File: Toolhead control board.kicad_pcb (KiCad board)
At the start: 2 copper layers, 52 x 45.8 mm, 77 parts, among them J1 Conn_01x02_Pin, J12 Conn_01x04_Male, J14 Conn_01x04_Male, J2 Conn_01x02_Pin, J3 Conn_01x02_Pin, J4 Conn_01x02_Pin, J5 Conn_01x02_Pin, J6 Conn_01x02_Pin, J7 USB_C_Receptacle_USB2.0_14P, Q1 AS3400, Q2 AS3400, Q3 AS3400, SW1 SW_SPST, SW2 SW_SPST, U1 ADXL345, U2 STM32F042G6Ux, U3 TMC2209, U4 AP63205WU, U5 MCP1802x-xx02xOT, U6 LP5907-2.5, Y1 8MHz

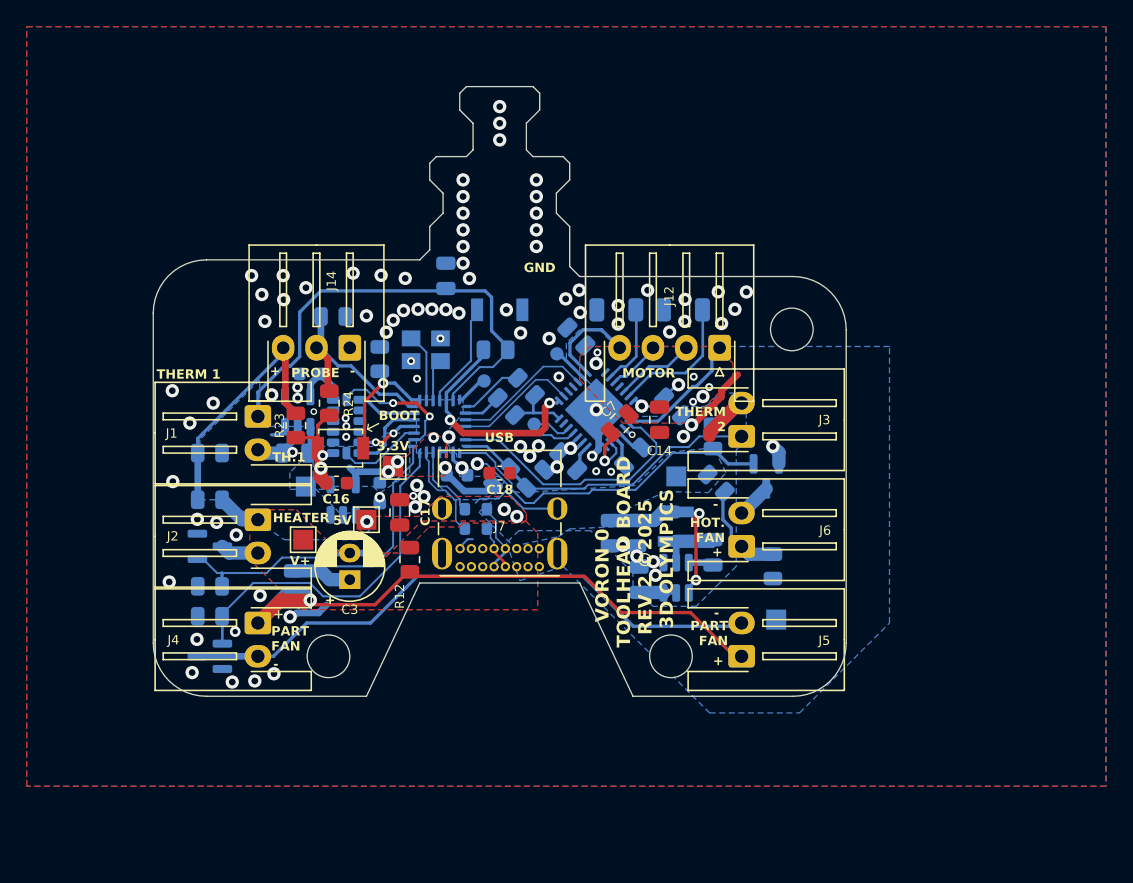
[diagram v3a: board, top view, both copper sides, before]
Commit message: Rev3 (connectors on back, and with USB daughter board) - probably done
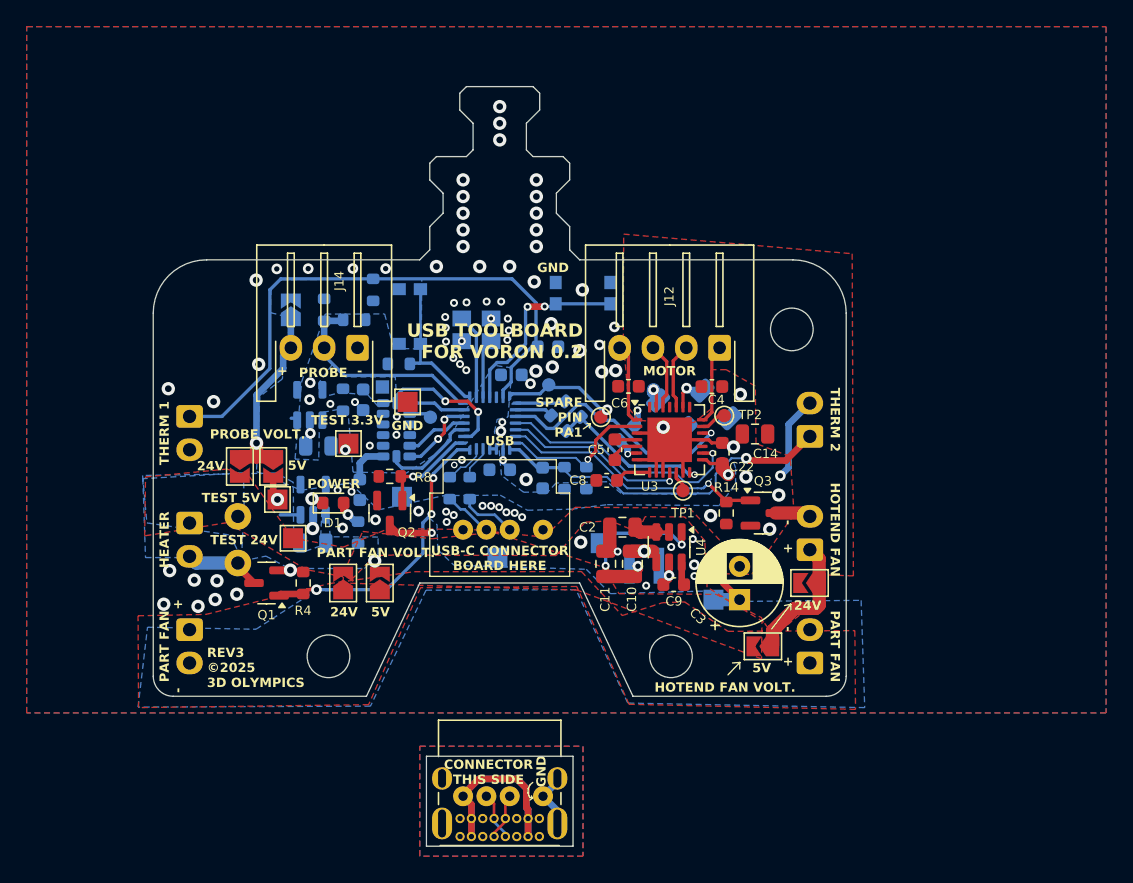
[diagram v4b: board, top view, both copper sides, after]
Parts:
- removed C18: 1uF, Capacitor_SMD:C_0603_1608Metric
- removed R16, R21, R22, R23, R24, R25: OPEN, Resistor_SMD:R_0805_2012Metric
- removed the REF** at (170.8, 97.2)
- removed the REF** at (135.4, 87.3)
- removed the REF** at (150.0, 67.0)
- removed the REF** at (163.2, 86.5)
- added C22: 1uF, Capacitor_SMD:C_0603_1608Metric, F.Cu at (166.7, 84.8)
- added D1: LED, LED_SMD:LED_0603_1608Metric, F.Cu at (137.5, 88.5)
- added J2: Conn_01x02_Pin, Connector_JST:JST_XH_B2B-XH-A_1x02_P2.50mm_Vertical, B.Cu at (126.7, 90.0)
- added JP11: SolderJumper_2_Open, Jumper:SolderJumper-2_P1.3mm_Open_TrianglePad1.0x1.5mm, F.Cu at (133.0, 85.8)
- added JP12: SolderJumper_2_Open, Jumper:SolderJumper-2_P1.3mm_Open_TrianglePad1.0x1.5mm, F.Cu at (130.5, 85.8)
- added JP5: SolderJumper_2_Open, Jumper:SolderJumper-2_P1.3mm_Open_TrianglePad1.0x1.5mm, F.Cu at (141.0, 94.5)
- added JP6: SolderJumper_2_Open, Jumper:SolderJumper-2_P1.3mm_Open_TrianglePad1.0x1.5mm, F.Cu at (138.2, 94.5)
- added JP7: SolderJumper_2_Open, Jumper:SolderJumper-2_P1.3mm_Open_TrianglePad1.0x1.5mm, F.Cu at (169.8, 99.2)
- added JP8: SolderJumper_2_Open, Jumper:SolderJumper-2_P1.3mm_Open_TrianglePad1.0x1.5mm, F.Cu at (173.2, 94.5)
- added JP9: SolderJumper_2_Open, Jumper:SolderJumper-2_P1.3mm_Open_TrianglePad1.0x1.5mm, B.Cu at (134.3, 74.0)
- added R10: OPEN, Resistor_SMD:R_0603_1608Metric, B.Cu at (139.4, 90.7)
- added R11: OPEN, Resistor_SMD:R_0603_1608Metric, B.Cu at (139.1, 74.8)
- added REF**: MountingHole_2.2mm_M2_DIN965_Pad, MountingHole:MountingHole_2.2mm_M2_DIN965_Pad, F.Cu at (153.2, 110.5)
- added REF**: TestPoint_Pad_1.5x1.5mm, TestPoint:TestPoint_Pad_1.5x1.5mm, F.Cu at (143.1, 80.9)
- added REF**: MountingHole_2.2mm_M2_DIN965_Pad, MountingHole:MountingHole_2.2mm_M2_DIN965_Pad, F.Cu at (153.2, 90.5)
- added REF**: MountingHole_2.2mm_M2_DIN965_Pad, MountingHole:MountingHole_2.2mm_M2_DIN965_Pad, F.Cu at (147.2, 110.5)
- added REF**: TestPoint_Pad_1.5x1.5mm, TestPoint:TestPoint_Pad_1.5x1.5mm, B.Cu at (157.6, 91.5)
- added REF**: TestPoint_Pad_1.0x1.0mm, TestPoint:TestPoint_Pad_1.0x1.0mm, B.Cu at (141.2, 79.8)
- added REF**: TestPoint_Pad_1.5x1.5mm, TestPoint:TestPoint_Pad_1.5x1.5mm, B.Cu at (149.8, 92.6)
- added REF**: MountingHole_2.2mm_M2_DIN965_Pad, MountingHole:MountingHole_2.2mm_M2_DIN965_Pad, F.Cu at (150.8, 110.5)
- added REF**: TestPoint_Pad_1.5x1.5mm, TestPoint:TestPoint_Pad_1.5x1.5mm, B.Cu at (142.7, 88.0)
- added REF**: TestPoint_Pad_1.5x1.5mm, TestPoint:TestPoint_Pad_1.5x1.5mm, B.Cu at (166.0, 95.8)
- added REF**: MountingHole_2.2mm_M2_DIN965_Pad, MountingHole:MountingHole_2.2mm_M2_DIN965_Pad, F.Cu at (149.0, 110.5)
- added REF**: MountingHole_2.2mm_M2_DIN965_Pad, MountingHole:MountingHole_2.2mm_M2_DIN965_Pad, F.Cu at (147.2, 90.5)
- added REF**: MountingHole_2.2mm_M2_DIN965_Pad, MountingHole:MountingHole_2.2mm_M2_DIN965_Pad, F.Cu at (149.0, 90.5)
- added REF**: MountingHole_2.2mm_M2_DIN965_Pad, MountingHole:MountingHole_2.2mm_M2_DIN965_Pad, F.Cu at (150.8, 90.5)
- added TP4: TestPoint_Probe, TestPoint:TestPoint_Pad_D1.0mm, B.Cu at (144.8, 82.1)
- added TP5: TestPoint_Probe, TestPoint:TestPoint_Pad_D1.0mm, F.Cu at (157.6, 82.0)
- C1, C13: value C -> 0.1uF; footprint Capacitor_SMD:C_0805_2012Metric -> Capacitor_SMD:C_0603_1608Metric
- C10, C11, Q1, Q2, Q3, TP1, TP2, U3, U4: moved to F.Cu
- C14: value 10uF -> 10uF 25V
- C16, C17: moved to B.Cu
- C2: value 10uF -> 10uF 25V; moved to F.Cu
- C3: footprint Capacitor_THT:CP_Radial_D5.0mm_P2.00mm -> Capacitor_THT:CP_Radial_D6.3mm_P2.50mm
- C4, C6: value 0.1uF -> 1uF; footprint Capacitor_SMD:C_0805_2012Metric -> Capacitor_SMD:C_0603_1608Metric; moved to F.Cu
- C5: value 22nF -> 22nF 50V; footprint Capacitor_SMD:C_0805_2012Metric -> Capacitor_SMD:C_0603_1608Metric; moved to F.Cu
- C7: value 0.1uF -> 0.1uF 25V; footprint Capacitor_SMD:C_0805_2012Metric -> Capacitor_SMD:C_0603_1608Metric; moved to B.Cu
- C8, C9: footprint Capacitor_SMD:C_0805_2012Metric -> Capacitor_SMD:C_0603_1608Metric; moved to F.Cu
- J1, J3, J4, J5, J6: footprint Connector_JST:JST_XH_S2B-XH-A-1_1x02_P2.50mm_Horizontal -> Connector_JST:JST_XH_B2B-XH-A_1x02_P2.50mm_Vertical; moved to B.Cu
- J2: footprint Connector_JST:JST_XH_S2B-XH-A-1_1x02_P2.50mm_Horizontal -> roLib2016:AK550_3.5mm_terminal_block; moved to B.Cu
- R1, R13, R3, R6, R7, R9: footprint Resistor_SMD:R_0805_2012Metric -> Resistor_SMD:R_0603_1608Metric
- R12: footprint Resistor_SMD:R_0805_2012Metric -> Resistor_SMD:R_0603_1608Metric; moved to B.Cu
- R14, R4, R8: footprint Resistor_SMD:R_0805_2012Metric -> Resistor_SMD:R_0603_1608Metric; moved to F.Cu
- R15: value OPEN -> 22k; footprint Resistor_SMD:R_0805_2012Metric -> Resistor_SMD:R_0603_1608Metric
- SW1: footprint Button_Switch_SMD:SW_SPST_B3U-1000P -> Button_Switch_SMD:SW_Push_1P1T_NO_CK_KMR2
- SW2: footprint Button_Switch_SMD:SW_SPST_B3U-1000P -> Button_Switch_SMD:SW_Push_1P1T_NO_CK_KMR2; moved to B.Cu
- U5: value MCP1802x-xx02xOT -> TPS7A2033
- U6: value LP5907-2.5 -> TPS7A2025
- moved C3 29.3 mm to (168.0, 95.8)
- moved J7 20.2 mm to (153.0, 113.5)
- moved R12 19.8 mm to (136.8, 74.0)
- moved Q2 17.3 mm to (141.8, 89.2), turned to -90 degrees
- moved R8 17.1 mm to (141.8, 86.5)
- moved C16 15.4 mm to (150.9, 78.9)
- moved R13 14.2 mm to (138.2, 80.8), turned to 90 degrees
- moved TP2 13.4 mm to (166.8, 81.9)
- moved TP1 12.2 mm to (163.8, 87.6)
- moved SW2 11.2 mm to (143.2, 74.5), turned to -90 degrees
- moved R19 10.3 mm to (166.2, 81.1), turned to -45 degrees
- moved R1 10.2 mm to (140.5, 72.5), turned to 90 degrees
- moved R15 9.76 mm to (156.5, 86.6), turned to 90 degrees
- moved C1 9.33 mm to (153.6, 76.8), turned to 0 degrees
- moved R18 7.87 mm to (162.9, 81.8), turned to -45 degrees
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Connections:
- C19 pad 1: +5V -> +3.3V
- R12 pad 1: +5V -> +3.3V
- R12 pad 2: Net-(J4-Pin_1) -> PROBE
- R13 pad 1: +VDC -> +3.3V
- R13 pad 2: Net-(J4-Pin_1) -> +2V5
- R15 pad 1: +5V -> +3.3V
- R15 pad 2: Net-(J6-Pin_1) -> E_ENN
- U1 pad 9: unconnected-(U1-INT2-Pad9) -> Net-(U1-INT2)
- U2 pad 13: E_EN -> HOTEND_FAN
- U2 pad 14: THERMISTOR_2 -> E_ENN
- U2 pad 15: HOTEND_FAN -> THERMISTOR_2
- U2 pad 21: PART_FAN -> HEATER
- U2 pad 22: HEATER -> PART_FAN
- U3 pad 1: Net-(J12-Pin_1) -> Net-(J12-Pin_4)
- U3 pad 13: /Stepper/CLK_IN -> GND
- U3 pad 2: E_EN -> E_ENN
- U3 pad 21: Net-(J12-Pin_4) -> Net-(J12-Pin_1)
- U3 pad 24: Net-(J12-Pin_3) -> Net-(J12-Pin_2)
- U3 pad 26: Net-(J12-Pin_2) -> Net-(J12-Pin_3)
- U6 pad 1: +5V -> +3.3V
- U6 pad 3: +5V -> +3.3V
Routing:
- net Net-(J4-Pin_1): track 46.0 -> 0.00 mm, vias 1 -> 0
- net Net-(J4-Pin_2): track 45.0 -> 3.39 mm, vias 0 -> 1
- net +3.3V: track 33.2 -> 6.82 mm, vias 8 -> 2
- net E_EN: track 20.1 -> 0.00 mm
- net PART_FAN: track 26.0 -> 7.59 mm, vias 0 -> 1
- net +VDC: track 15.0 -> 32.9 mm, vias 8 -> 1
- net GND: track 50.0 -> 34.0 mm, vias 101 -> 104
- net E_ENN: track 0.00 -> 11.2 mm, vias 0 -> 1
- net E_STEP: track 9.33 -> 18.9 mm, vias 0 -> 1
- net E_DIR: track 10.6 -> 18.6 mm, vias 0 -> 1
- net Net-(U3-BRB): track 10.2 -> 2.33 mm, vias 0 -> 1
- net Net-(SW1-B): track 7.20 -> 14.7 mm, vias 0 -> 2
- net THERMISTOR_1: track 35.2 -> 42.6 mm
- net UART: track 4.95 -> 11.9 mm, vias 0 -> 1
- net Net-(U2-PA1): track 2.42 -> 9.20 mm, vias 0 -> 1
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- added copper zone on B.Cu, net +2V5
- added copper zone on F.Cu, net Net-(J4-Pin_1)
- added copper zone on B.Cu, net Net-(J4-Pin_2)
- removed copper zone on F.Cu, net +3.3V
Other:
- board size 52 x 45.8 mm -> 52 x 57 mm
- board text added: "2.5V"
- board text added: "24V"
- board text added: "CONNECTOR THIS SIDE"
- board text added: "HOTEND FAN VOLT."
- board text added: "INT2"
- board text added: "LEGS THIS SIDE"
- board text added: "PA1 SPARE PIN"
- board text added: "PART FAN VOLT."
- board text added: "POWER"
- board text added: "PROBE 3.3V"
- board text added: "PROBE VOLT."
- board text added: "REV3 ©2025 3D OLYMPICS"
- board text added: "SPARE PIN PA1"
- board text added: "TEST 24V"
- board text added: "TEST 3.3V"
- board text added: "TEST 5V"
- board text added: "USB TOOLBOARD FOR VORON 0.2"
- board text added: "USB-C CONNECTOR BOARD HERE"
- board text added: "{dblquote}ENDSTOP{dblquote} PARTS ON TOP OF X BEAM"
- board text removed: "3.3V"
- board text removed: "HOT. FAN"
- board text removed: "P.FAN"
- board text removed: "TH.1"
- board text removed: "V+"
- board text removed: "VORON 0 TOOLHEAD BOARD REV 2 ©2025 3D OLYMPICS"
